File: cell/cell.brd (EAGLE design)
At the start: 35.6 x 48.3 mm, 11 parts

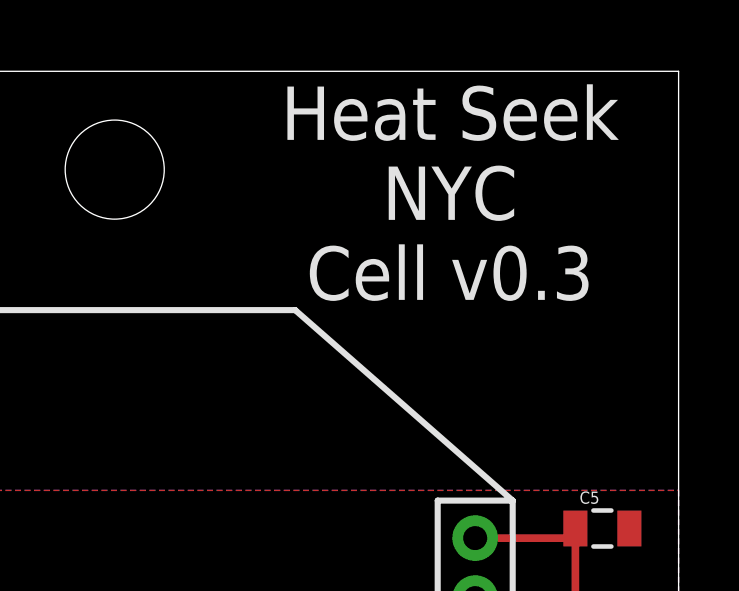
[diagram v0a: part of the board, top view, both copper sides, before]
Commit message: ground DIN/!CONFIG so that we can safely disable its pullup resistor
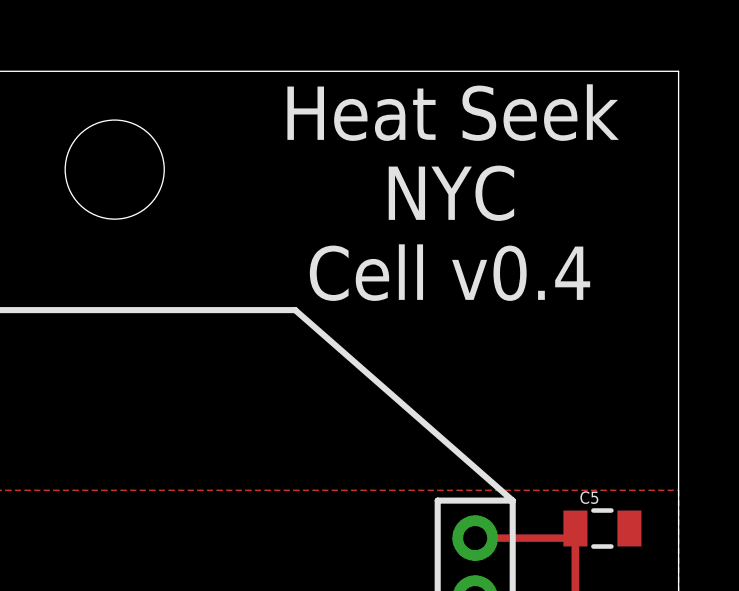
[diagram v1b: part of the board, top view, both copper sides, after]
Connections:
- net GND: now also XB24.3
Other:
- board text added: "Heat Seek NYC Cell v0.4"
- board text removed: "Heat Seek NYC Cell v0.3"
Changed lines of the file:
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@@
 <text x="27.94" y="40.64" size="1.778" layer="21" font="vector" ratio="15" align="bottom-center">Heat Seek
 NYC
-Cell v0.3</text>
+Cell v0.4</text>
 <text x="26.67" y="59.69" size="1.778" layer="51" font="vector" ratio="15">Harold Cooper</text>
 </plain>
@@
 <contactref element="MCP9700A" pad="3"/>
 <contactref element="XB24" pad="10"/>
+<contactref element="XB24" pad="3"/>
 </signal>
 <signal name="V_BATT">

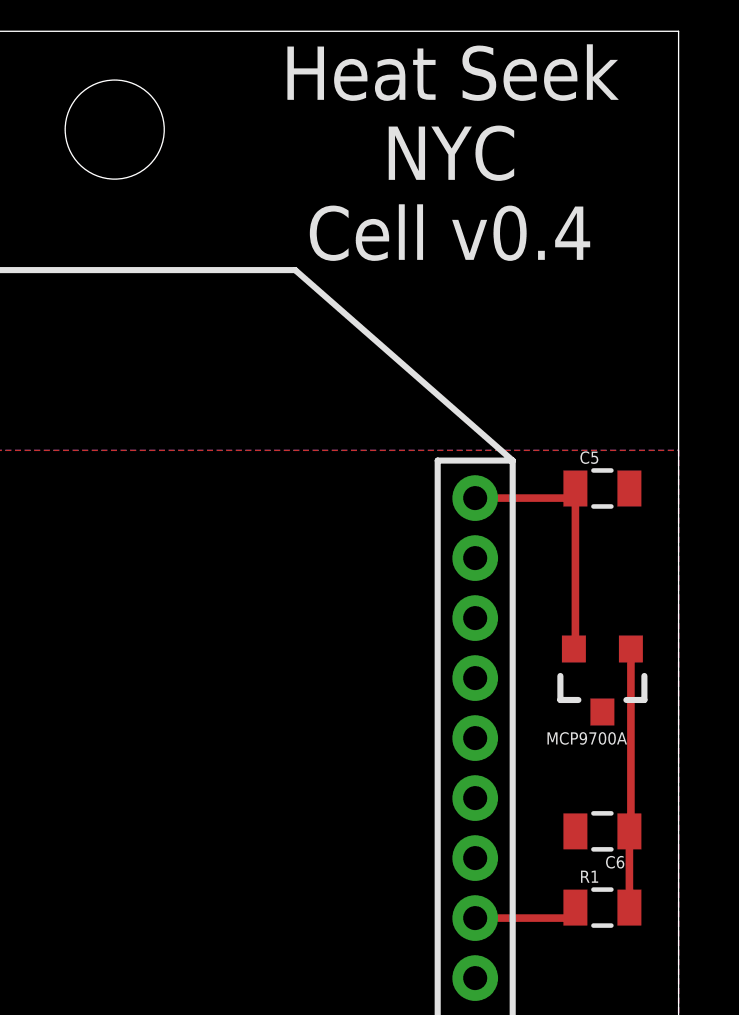
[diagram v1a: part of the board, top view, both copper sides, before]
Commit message: replace MCP9700A with LMT70
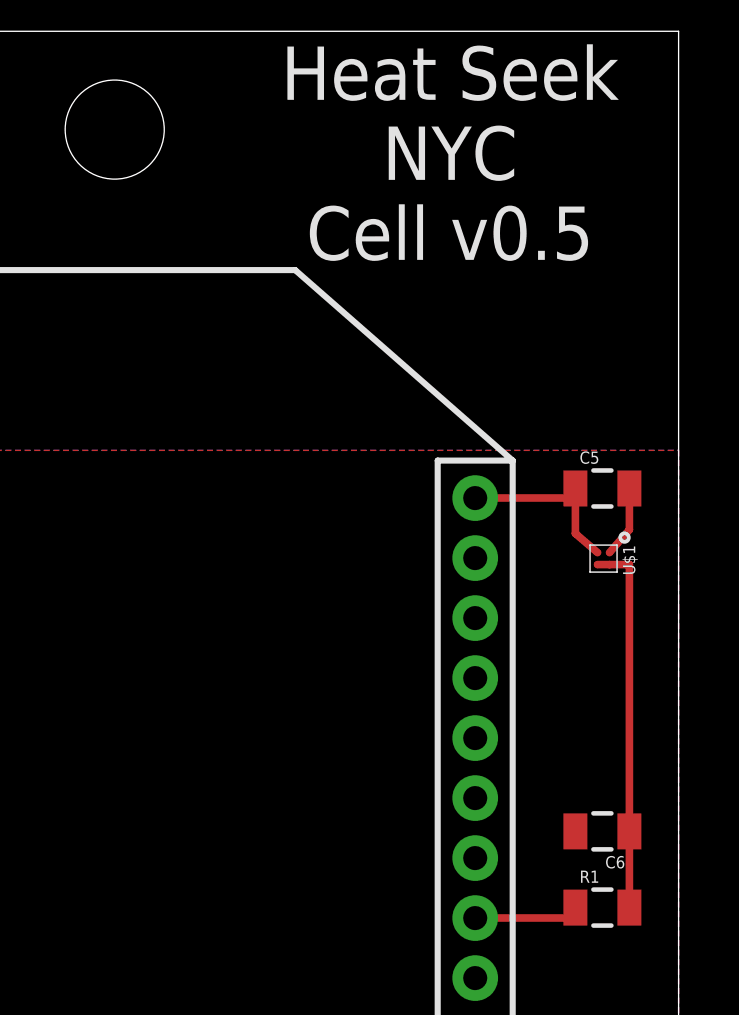
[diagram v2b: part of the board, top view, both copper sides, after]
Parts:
- removed MCP9700A: MCP9700SMD, SparkFun-Sensors:SOT23-3
- added U$1: LMT40, lmt40:YFP0004
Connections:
- removed net N$3: C5.1, MCP9700A.2, XB24.20
- new net N$7: C5.1, U$1.TAO, XB24.20
- net GND: now also U$1.GND; no longer MCP9700A.3
- net N$1: now also U$1.T_ON, U$1.VDD; no longer MCP9700A.1
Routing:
- net N$3: track 9.06 -> 0.00 mm
- net N$7: track 0.00 -> 6.14 mm
- net N$1: track 8.67 -> 12.5 mm
- net GND: track 0.00 -> 2.38 mm
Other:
- board text added: "Harold Cooper, Doyun Kim"
- board text added: "Heat Seek NYC Cell v0.5"
- board text removed: "Harold Cooper"
- board text removed: "Heat Seek NYC Cell v0.4"
